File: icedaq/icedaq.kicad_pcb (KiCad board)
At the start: 2 copper layers, 64 x 55 mm, 68 parts, among them J1 analog outputs, J2 analog inputs, P1 UART, P2 GPIO, U1 REG12, U2 iCE40HX1K-VQ100, U3 RPi, U4 oscillator4, U5 ADC082S021, U6 ADC082S021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

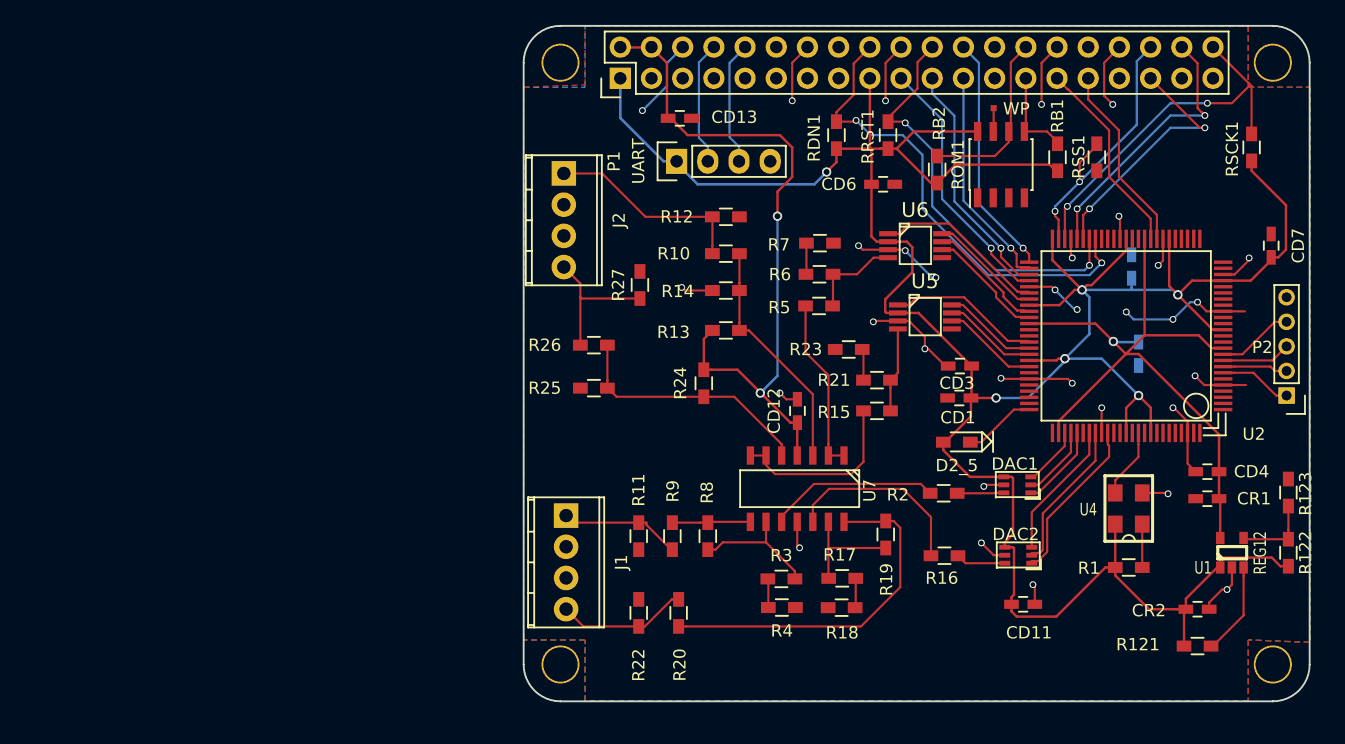
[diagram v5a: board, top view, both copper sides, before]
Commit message: icedaq: relocate connectors
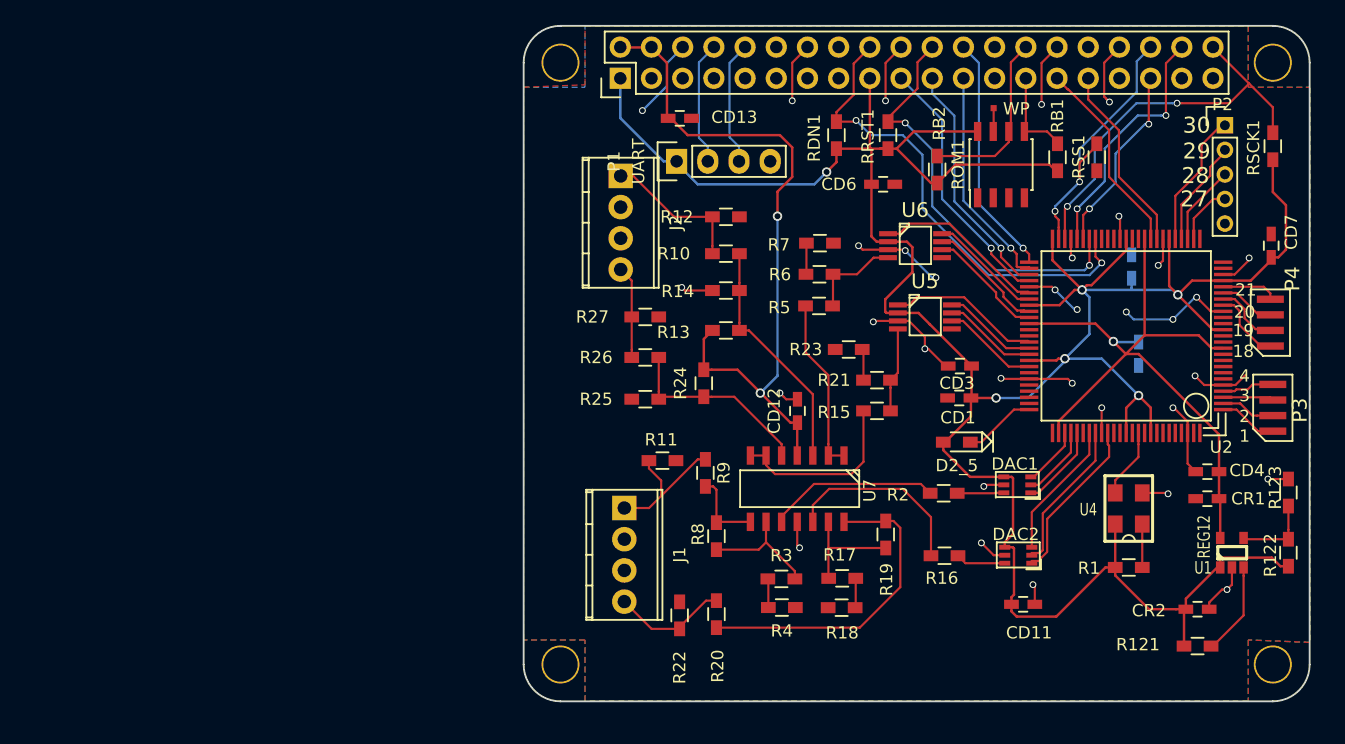
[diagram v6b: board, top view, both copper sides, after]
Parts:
- added P3: GPIO2, local:gpio, F.Cu at (198.0, 86.1)
- added P4: GPIO3, local:gpio, F.Cu at (197.8, 79.2)
- moved P2 22.6 mm to (194.1, 63.1), turned to 0 degrees
- moved R11 6.45 mm to (148.3, 90.4), turned to 180 degrees
- moved R9 5.81 mm to (151.8, 91.4), turned to 270 degrees
- moved J1 4.78 mm to (145.2, 94.3)
- moved J2 4.63 mm to (144.9, 67.2)
- moved R26 4.30 mm to (146.9, 82.0)
- moved R25 4.28 mm to (146.9, 85.4)
- moved R22 3.34 mm to (149.7, 103.0)
- moved R20 3.08 mm to (152.7, 102.9)
- moved R27 2.64 mm to (146.9, 78.7), turned to 180 degrees
- moved RSCK1 1.73 mm to (198.0, 64.8)
- moved R8 0.70 mm to (152.7, 96.5)
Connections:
- U2 pad 10: Net-(P2-Pad4) -> Net-(U2-Pad10)
- U2 pad 27: Net-(U2-Pad27) -> Net-(P2-Pad4)
- U2 pad 28: Net-(U2-Pad28) -> Net-(P2-Pad3)
- U2 pad 29: Net-(U2-Pad29) -> Net-(P2-Pad2)
- U2 pad 30: Net-(U2-Pad30) -> Net-(P2-Pad1)
- U2 pad 7: Net-(P2-Pad1) -> Net-(U2-Pad7)
- U2 pad 8: Net-(P2-Pad2) -> Net-(U2-Pad8)
- U2 pad 9: Net-(P2-Pad3) -> Net-(U2-Pad9)
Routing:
- net Net-(P4-Pad1): track 0.00 -> 5.89 mm
- net /MISO: track 20.9 -> 15.5 mm
- net Net-(P4-Pad2): track 0.00 -> 5.33 mm
- net Net-(P2-Pad1): track 5.93 -> 11.1 mm
- net Net-(P3-Pad1): track 0.00 -> 4.82 mm
- net /Analog/in1: track 16.6 -> 11.8 mm
- net Net-(P4-Pad3): track 0.00 -> 4.58 mm
- net Net-(P4-Pad4): track 0.00 -> 4.54 mm
- net Net-(R24-Pad1): track 20.5 -> 16.0 mm
- net Net-(P3-Pad2): track 0.00 -> 4.45 mm
- net /Analog/in3: track 11.8 -> 7.53 mm
- net Net-(P3-Pad4): track 0.00 -> 4.27 mm
- net Net-(P3-Pad3): track 0.00 -> 4.13 mm
- net Net-(P2-Pad2): track 5.31 -> 8.71 mm
- net Net-(R19-Pad2): track 29.0 -> 26.0 mm
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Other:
- rule pad_to_mask_clearance: 0.2 -> 0.1
- board text added: "1"
- board text added: "18"
- board text added: "19"
- board text added: "2"
- board text added: "20"
- board text added: "21"
- board text added: "27"
- board text added: "28"
- board text added: "29"
- board text added: "3"
- board text added: "30"
- board text added: "4"

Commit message: icedaq rev 1
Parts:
- added REF**: Symbol_CC-PublicDomain_SilkScreenTop_Big, Symbols:Symbol_CC-PublicDomain_SilkScreenTop_Big, B.Cu at (159.5, 92.6)
- added REF***: KiCad-Logo_6mm_SilkScreen, Symbols:KiCad-Logo_6mm_SilkScreen, B.Cu at (176.1, 93.1)
- added REF***: OSHW-Logo_5.7x6mm_SilkScreen, Symbols:OSHW-Logo_5.7x6mm_SilkScreen, B.Cu at (191.6, 100.2)
- added REF***: WEEE-Logo_4.2x6mm_SilkScreen, Symbols:WEEE-Logo_4.2x6mm_SilkScreen, B.Cu at (191.5, 91.8)
- P2: value GPIO -> GPIO0; footprint Pin_Headers:Pin_Header_Straight_1x05_Pitch2.00mm -> Pin_Headers:Pin_Header_Straight_2x03
- moved R27 6.22 mm to (142.5, 83.1), turned to 90 degrees
- moved J2 4.08 mm to (147.3, 70.5)
- moved J1 3.98 mm to (147.7, 91.2)
- moved R11 2.30 mm to (148.3, 88.1), turned to 0 degrees
- moved P2 1.90 mm to (193.5, 64.9), turned to 270 degrees
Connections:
- U2 pad 27: Net-(P2-Pad4) -> Net-(P2-Pad2)
- U2 pad 28: Net-(P2-Pad3) -> Net-(P2-Pad1)
- U2 pad 29: Net-(P2-Pad2) -> Net-(P2-Pad4)
- U2 pad 30: Net-(P2-Pad1) -> Net-(P2-Pad3)
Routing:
- net /Analog/out3: track 11.5 -> 6.66 mm
- net /Analog/in1: track 11.8 -> 8.08 mm
- net Net-(P2-Pad2): track 8.71 -> 5.71 mm
- net Net-(P2-Pad1): track 11.1 -> 9.07 mm
- net Net-(P2-Pad3): track 6.50 -> 8.12 mm
- net /Analog/out4: track 9.46 -> 10.6 mm
- net GND: track 103.8 -> 102.8 mm
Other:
- board text added: "90"
- board text added: "MAD 2017"
- board text added: "iCE40 Analog I/O Hat"
- board text added: "in1"
- board text added: "in2"
- board text added: "out1"
- board text added: "out2"
- board text removed: "19"
- board text removed: "2"
- board text removed: "20"
- board text removed: "3"
